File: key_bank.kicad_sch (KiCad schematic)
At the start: 2 parts, among them U4 MCP3208

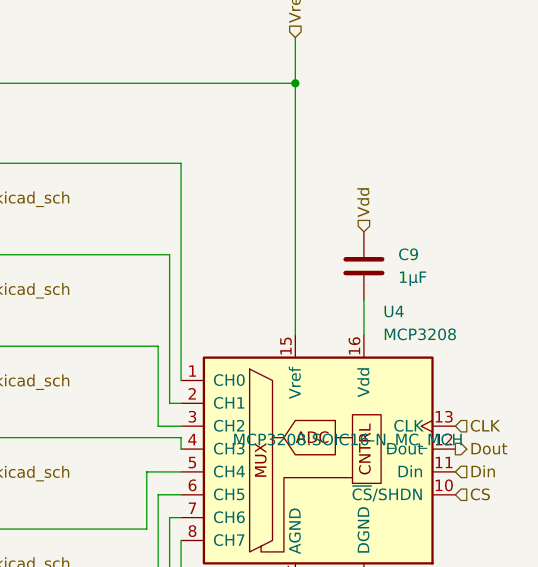
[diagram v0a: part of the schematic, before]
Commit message: [ADD](keys) added keys subsheet
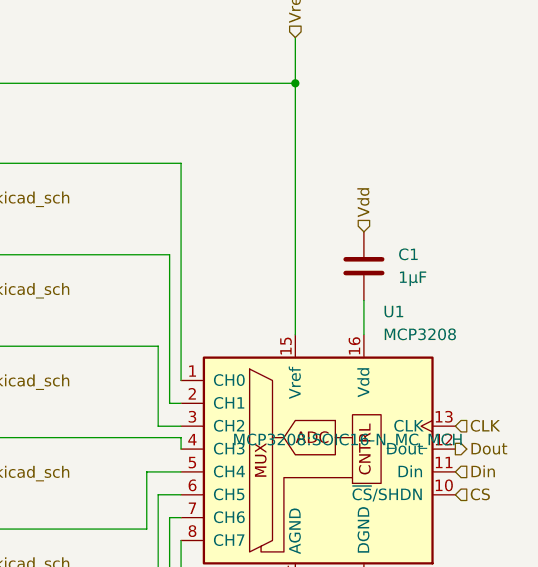
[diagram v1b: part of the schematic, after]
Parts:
- renumbered C9 to C1, U4 to U1

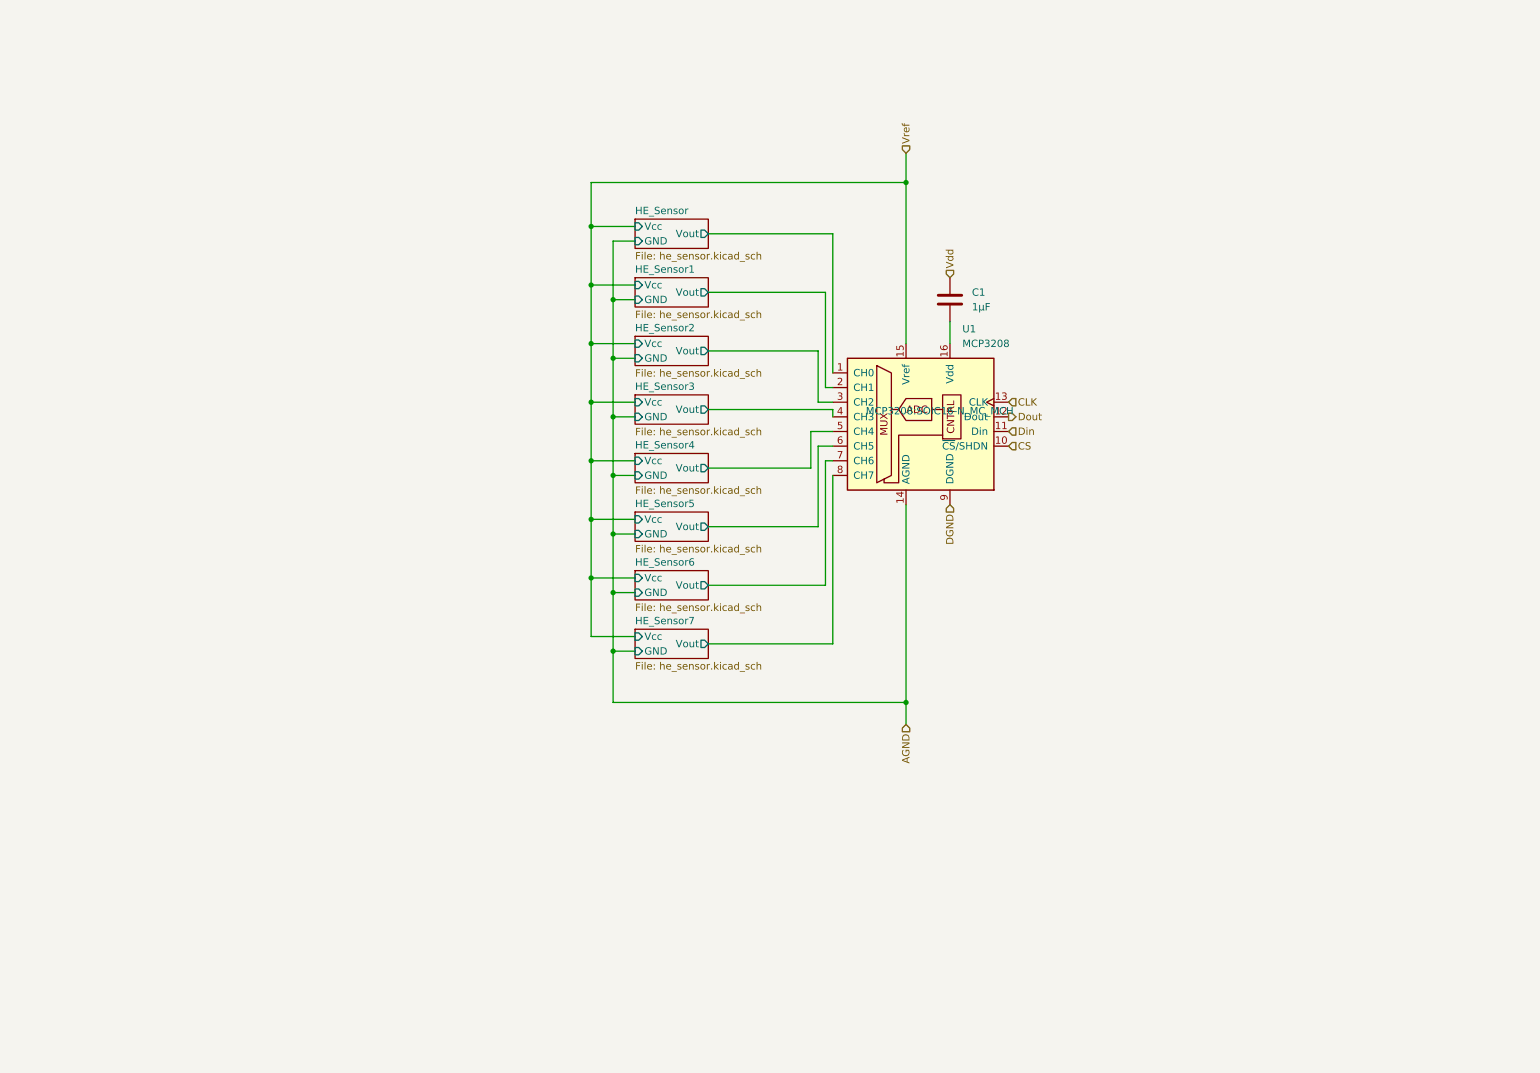
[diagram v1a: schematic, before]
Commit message: [UPDATE](TMR) switched to TMR sensors + added ldo
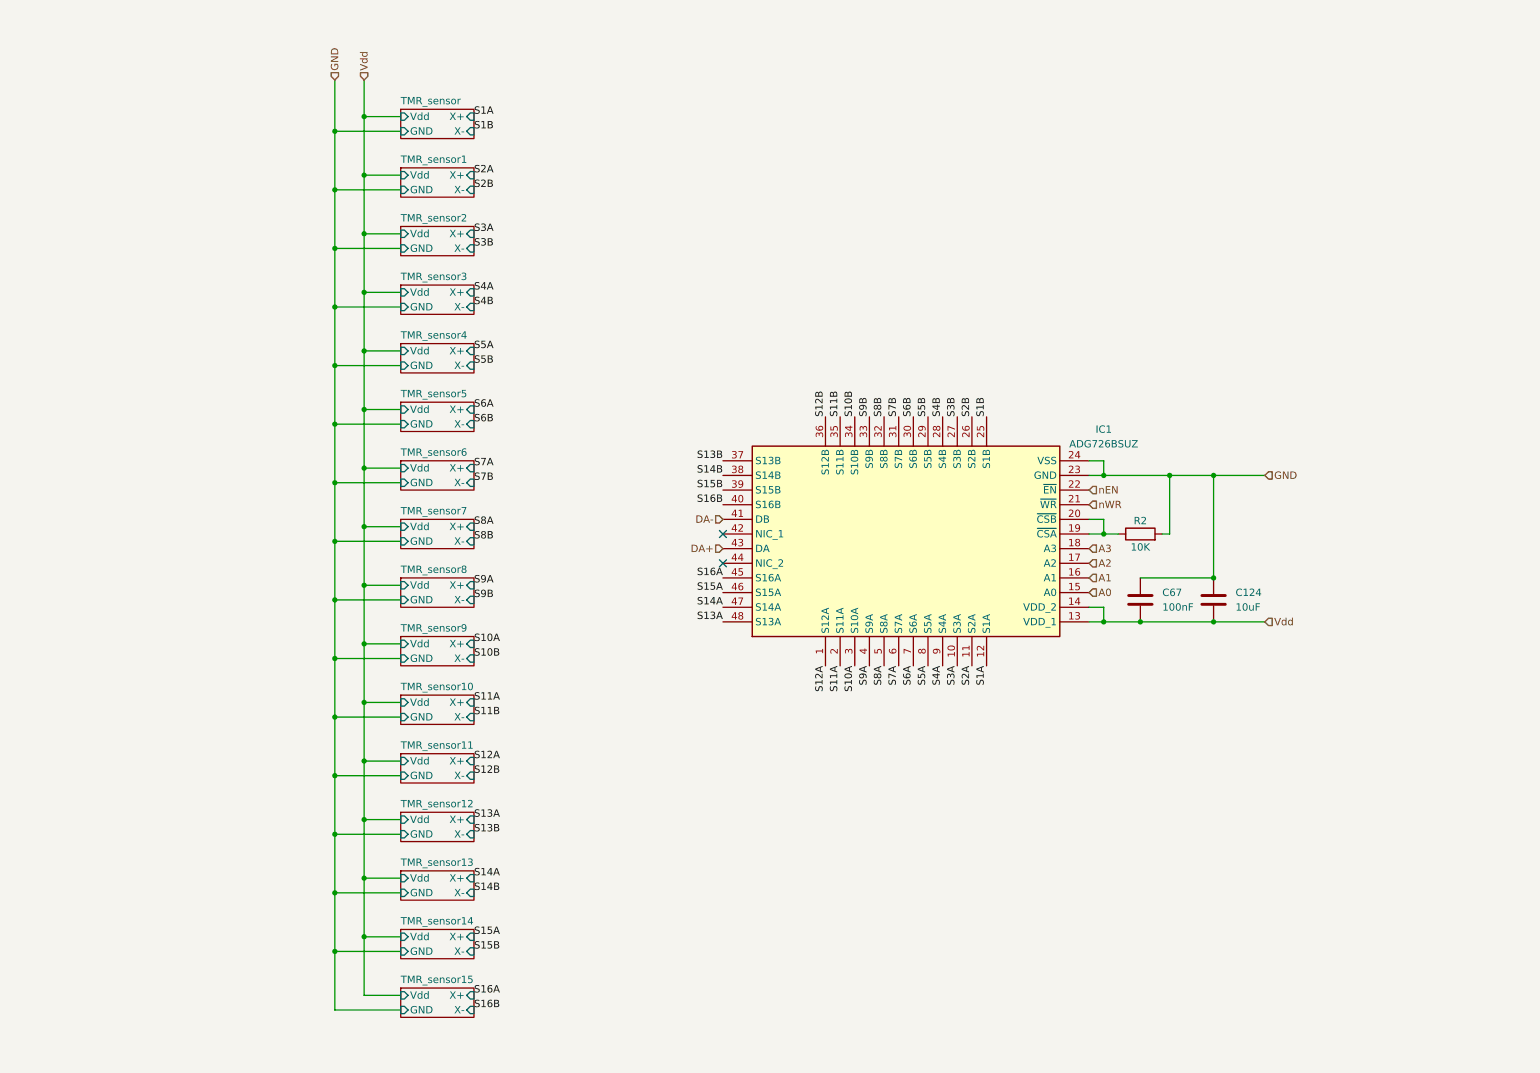
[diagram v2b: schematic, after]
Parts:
- removed C1: 1µF, symbol Device:C
- removed U1: MCP3208, MCP3208:SOIC16-N_MC_MCH, symbol Analog_ADC:MCP3208
- added C124: 10uF, symbol Device:C
- added C67: 100nF, symbol Device:C
- added IC1: ADG726BSUZ, QFP50P900X900X120-48N, symbol ADG726BSUZ:ADG726BSUZ
- added R2: 10K, symbol Device:R
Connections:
- net Vdd: now also C124.2, C67.2, IC1.13 (VDD_1), IC1.14 (VDD_2)
- new net: IC1.19 (~{CSA}), IC1.20 (~{CSB}), R2.1
- new net A0: IC1.15 (A0)
- new net A1: IC1.16 (A1)
- new net A2: IC1.17 (A2)
- new net A3: IC1.18 (A3)
- new net DA+: IC1.43 (DA)
- new net DA-: IC1.41 (DB)
- new net GND: C124.1, C67.1, IC1.23 (GND), IC1.24 (VSS), R2.2
- new net S10A: IC1.3 (S10A)
- new net S10B: IC1.34 (S10B)
- new net S11A: IC1.2 (S11A)
- new net S11B: IC1.35 (S11B)
- new net S12A: IC1.1 (S12A)
- new net S12B: IC1.36 (S12B)
- new net S13A: IC1.48 (S13A)
- new net S13B: IC1.37 (S13B)
- new net S14A: IC1.47 (S14A)
- new net S14B: IC1.38 (S14B)
- new net S15A: IC1.46 (S15A)
- new net S15B: IC1.39 (S15B)
- new net S16A: IC1.45 (S16A)
- new net S16B: IC1.40 (S16B)
- new net S1A: IC1.12 (S1A)
- new net S1B: IC1.25 (S1B)
- new net S2A: IC1.11 (S2A)
- new net S2B: IC1.26 (S2B)
- new net S3A: IC1.10 (S3A)
- new net S3B: IC1.27 (S3B)
- new net S4A: IC1.9 (S4A)
- new net S4B: IC1.28 (S4B)
- new net S5A: IC1.8 (S5A)
- new net S5B: IC1.29 (S5B)
- new net S6A: IC1.7 (S6A)
- new net S6B: IC1.30 (S6B)
- new net S7A: IC1.6 (S7A)
- new net S7B: IC1.31 (S7B)
- new net S8A: IC1.5 (S8A)
- new net S8B: IC1.32 (S8B)
- new net S9A: IC1.4 (S9A)
- new net S9B: IC1.33 (S9B)
- new net nEN: IC1.22 (~{EN})
- new net nWR: IC1.21 (~{WR})
- no-connect marks 0 -> 2
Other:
- removed sheet HE_Sensor
- removed sheet HE_Sensor1
- removed sheet HE_Sensor2
- removed sheet HE_Sensor3
- removed sheet HE_Sensor4
- removed sheet HE_Sensor5
- removed sheet HE_Sensor6
- removed sheet HE_Sensor7
- added sheet TMR_sensor (he_sensor.kicad_sch)
- added sheet TMR_sensor1 (he_sensor.kicad_sch)
- added sheet TMR_sensor10 (he_sensor.kicad_sch)
- added sheet TMR_sensor11 (he_sensor.kicad_sch)
- added sheet TMR_sensor12 (he_sensor.kicad_sch)
- added sheet TMR_sensor13 (he_sensor.kicad_sch)
- added sheet TMR_sensor14 (he_sensor.kicad_sch)
- added sheet TMR_sensor15 (he_sensor.kicad_sch)
- added sheet TMR_sensor2 (he_sensor.kicad_sch)
- added sheet TMR_sensor3 (he_sensor.kicad_sch)
- added sheet TMR_sensor4 (he_sensor.kicad_sch)
- added sheet TMR_sensor5 (he_sensor.kicad_sch)
- added sheet TMR_sensor6 (he_sensor.kicad_sch)
- added sheet TMR_sensor7 (he_sensor.kicad_sch)
- added sheet TMR_sensor8 (he_sensor.kicad_sch)
- added sheet TMR_sensor9 (he_sensor.kicad_sch)

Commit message: [ADD](General) v1
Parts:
- renumbered C67 to C14, C124 to C15, IC1 to IC2, R2 to R4
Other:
- note added: "Analog multiplexer"
- note added: "TMR sensors"
- company: (none) -> Ryzzen
- title: (none) -> TMR based triple USB Keyboard
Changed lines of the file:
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@@
 	(generator_version "9.0")
 	(paper "A4")
+	(title_block
+		(title "TMR based triple USB Keyboard")
+		(date "2025-12-28")
+		(rev "v1")
+		(company "Ryzzen")
+	)
+	(rectangle
+		(start 59.69 15.24)
+		(end 100.33 193.04)
+		(stroke
+			(width 0)
+			(type default)
+		)
+		(fill
+			(type none)
+		)
+	)
+	(rectangle
+		(start 123.19 72.39)
+		(end 237.49 138.43)
+		(stroke
+			(width 0)
+			(type default)
+		)
+		(fill
+			(type none)
+		)
+	)
+	(text "TMR sensors"
+		(exclude_from_sim no)
+		(at 110.998 17.018 0)
+		(effects
+			(font
+				(size 1.905 1.905)
+				(thickness 0.381)
+				(bold yes)
+			)
+		)
+	)
+	(text "Analog multiplexer"
+		(exclude_from_sim no)
+		(at 136.652 70.104 0)
+		(effects
+			(font
+				(size 1.905 1.905)
+				(thickness 0.381)
+				(bold yes)
+			)
+		)
+	)
 	(junction
 		(at 66.04 115.57)
@@
 		(dnp no)
 		(fields_autoplaced yes)
-		(property "Reference" "IC1"
+		(property "Reference" "IC2"
 			(at 199.39 85.9946 90)
 			(effects
@@
 				)
 				(path "/5d44d704-6136-40a8-98a4-93f001ea8743/c5dd3d76-8c7d-4253-bbc0-6b560edbfa92/3892192a-9e74-4718-aa5a-d4dfa6dc670f"
+					(reference "IC4")
+					(unit 1)
+				)
+				(path "/5d44d704-6136-40a8-98a4-93f001ea8743/c5dd3d76-8c7d-4253-bbc0-6b560edbfa92/735f3a62-f16a-407d-b596-d90350aa3066"
+					(reference "IC23")
+					(unit 1)
+				)
+				(path "/5d44d704-6136-40a8-98a4-93f001ea8743/c5dd3d76-8c7d-4253-bbc0-6b560edbfa92/7ffe2115-dd72-444b-89b3-b9005c9fe688"
+					(reference "IC44")
+					(unit 1)
+				)
+				(path "/5d44d704-6136-40a8-98a4-93f001ea8743/c5dd3d76-8c7d-4253-bbc0-6b560edbfa92/a1b59adb-224c-4a31-865b-1e7950bd0f40"
 					(reference "IC2")
 					(unit 1)
 				)
-				(path "/5d44d704-6136-40a8-98a4-93f001ea8743/c5dd3d76-8c7d-4253-bbc0-6b560edbfa92/735f3a62-f16a-407d-b596-d90350aa3066"
-					(reference "IC21")
-					(unit 1)
-				)
-				(path "/5d44d704-6136-40a8-98a4-93f001ea8743/c5dd3d76-8c7d-4253-bbc0-6b560edbfa92/7ffe2115-dd72-444b-89b3-b9005c9fe688"
-					(reference "IC22")
-					(unit 1)
-				)
-				(path "/5d44d704-6136-40a8-98a4-93f001ea8743/c5dd3d76-8c7d-4253-bbc0-6b560edbfa92/a1b59adb-224c-4a31-865b-1e7950bd0f40"
-					(reference "IC1")
-					(unit 1)
-				)
 				(path "/5d44d704-6136-40a8-98a4-93f001ea8743/c5dd3d76-8c7d-4253-bbc0-6b560edbfa92/cc77bec8-d3cc-43bb-b7a5-b3b6cadba114"
-					(reference "IC62")
+					(reference "IC78")
 					(unit 1)
 				)
@@
 		(on_board yes)
 		(dnp no)
-		(property "Reference" "R2"
+		(property "Reference" "R4"
 			(at 205.74 101.854 90)
 			(effects
@@
 			(project ""
 				(path "/5d44d704-6136-40a8-98a4-93f001ea8743/c5dd3d76-8c7d-4253-bbc0-6b560edbfa92/13b615a6-6b6e-4376-a5a5-45c5057b142a"
+					(reference "R8")
+					(unit 1)
+				)
+				(path "/5d44d704-6136-40a8-98a4-93f001ea8743/c5dd3d76-8c7d-4253-bbc0-6b560edbfa92/3892192a-9e74-4718-aa5a-d4dfa6dc670f"
+					(reference "R5")
+					(unit 1)
+				)
+				(path "/5d44d704-6136-40a8-98a4-93f001ea8743/c5dd3d76-8c7d-4253-bbc0-6b560edbfa92/735f3a62-f16a-407d-b596-d90350aa3066"
 					(reference "R6")
 					(unit 1)
 				)
-				(path "/5d44d704-6136-40a8-98a4-93f001ea8743/c5dd3d76-8c7d-4253-bbc0-6b560edbfa92/3892192a-9e74-4718-aa5a-d4dfa6dc670f"
-					(reference "R3")
+				(path "/5d44d704-6136-40a8-98a4-93f001ea8743/c5dd3d76-8c7d-4253-bbc0-6b560edbfa92/7ffe2115-dd72-444b-89b3-b9005c9fe688"
+					(reference "R7")
 					(unit 1)
 				)
-				(path "/5d44d704-6136-40a8-98a4-93f001ea8743/c5dd3d76-8c7d-4253-bbc0-6b560edbfa92/735f3a62-f16a-407d-b596-d90350aa3066"
+				(path "/5d44d704-6136-40a8-98a4-93f001ea8743/c5dd3d76-8c7d-4253-bbc0-6b560edbfa92/a1b59adb-224c-4a31-865b-1e7950bd0f40"
 					(reference "R4")
 					(unit 1)
 				)
-				(path "/5d44d704-6136-40a8-98a4-93f001ea8743/c5dd3d76-8c7d-4253-bbc0-6b560edbfa92/7ffe2115-dd72-444b-89b3-b9005c9fe688"
-					(reference "R5")
-					(unit 1)
-				)
-				(path "/5d44d704-6136-40a8-98a4-93f001ea8743/c5dd3d76-8c7d-4253-bbc0-6b560edbfa92/a1b59adb-224c-4a31-865b-1e7950bd0f40"
-					(reference "R2")
-					(unit 1)
-				)
 				(path "/5d44d704-6136-40a8-98a4-93f001ea8743/c5dd3d76-8c7d-4253-bbc0-6b560edbfa92/cc77bec8-d3cc-43bb-b7a5-b3b6cadba114"
-					(reference "R7")
+					(reference "R9")
 					(unit 1)
 				)
@@
 		(dnp no)
 		(fields_autoplaced yes)
-		(property "Reference" "C124"
+		(property "Reference" "C15"
 			(at 222.25 114.2999 0)
 			(effects
@@
 			(project "RyzzenKeyboard"
 				(path "/5d44d704-6136-40a8-98a4-93f001ea8743/c5dd3d76-8c7d-4253-bbc0-6b560edbfa92/13b615a6-6b6e-4376-a5a5-45c5057b142a"
-					(reference "C128")
+					(reference "C78")
 					(unit 1)
 				)
 				(path "/5d44d704-6136-40a8-98a4-93f001ea8743/c5dd3d76-8c7d-4253-bbc0-6b560edbfa92/3892192a-9e74-4718-aa5a-d4dfa6dc670f"
-					(reference "C125")
+					(reference "C18")
 					(unit 1)
 				)
 				(path "/5d44d704-6136-40a8-98a4-93f001ea8743/c5dd3d76-8c7d-4253-bbc0-6b560edbfa92/735f3a62-f16a-407d-b596-d90350aa3066"
-					(reference "C126")
+					(reference "C38")
 					(unit 1)
 				)
 				(path "/5d44d704-6136-40a8-98a4-93f001ea8743/c5dd3d76-8c7d-4253-bbc0-6b560edbfa92/7ffe2115-dd72-444b-89b3-b9005c9fe688"
-					(reference "C127")
+					(reference "C60")
 					(unit 1)
 				)
 				(path "/5d44d704-6136-40a8-98a4-93f001ea8743/c5dd3d76-8c7d-4253-bbc0-6b560edbfa92/a1b59adb-224c-4a31-865b-1e7950bd0f40"
-					(reference "C124")
+					(reference "C15")
 					(unit 1)
 				)
 				(path "/5d44d704-6136-40a8-98a4-93f001ea8743/c5dd3d76-8c7d-4253-bbc0-6b560edbfa92/cc77bec8-d3cc-43bb-b7a5-b3b6cadba114"
-					(reference "C129")
+					(reference "C96")
 					(unit 1)
 				)
@@
 		(dnp no)
 		(fields_autoplaced yes)
-		(property "Reference" "C67"
+		(property "Reference" "C14"
 			(at 209.55 114.2999 0)
 			(effects
@@
 			(project "RyzzenKeyboard"
 				(path "/5d44d704-6136-40a8-98a4-93f001ea8743/c5dd3d76-8c7d-4253-bbc0-6b560edbfa92/13b615a6-6b6e-4376-a5a5-45c5057b142a"
-					(reference "C122")
+					(reference "C77")
 					(unit 1)
 				)
 				(path "/5d44d704-6136-40a8-98a4-93f001ea8743/c5dd3d76-8c7d-4253-bbc0-6b560edbfa92/3892192a-9e74-4718-aa5a-d4dfa6dc670f"
-					(reference "C68")
+					(reference "C17")
 					(unit 1)
 				)
 				(path "/5d44d704-6136-40a8-98a4-93f001ea8743/c5dd3d76-8c7d-4253-bbc0-6b560edbfa92/735f3a62-f16a-407d-b596-d90350aa3066"
-					(reference "C120")
+					(reference "C37")
 					(unit 1)
 				)
 				(path "/5d44d704-6136-40a8-98a4-93f001ea8743/c5dd3d76-8c7d-4253-bbc0-6b560edbfa92/7ffe2115-dd72-444b-89b3-b9005c9fe688"
-					(reference "C121")
+					(reference "C59")
 					(unit 1)
 				)
 				(path "/5d44d704-6136-40a8-98a4-93f001ea8743/c5dd3d76-8c7d-4253-bbc0-6b560edbfa92/a1b59adb-224c-4a31-865b-1e7950bd0f40"
-					(reference "C67")
+					(reference "C14")
 					(unit 1)
 				)
 				(path "/5d44d704-6136-40a8-98a4-93f001ea8743/c5dd3d76-8c7d-4253-bbc0-6b560edbfa92/cc77bec8-d3cc-43bb-b7a5-b3b6cadba114"
-					(reference "C123")
+					(reference "C95")
 					(unit 1)
 				)
@@
 			(project "RyzzenKeyboard"
 				(path "/5d44d704-6136-40a8-98a4-93f001ea8743/c5dd3d76-8c7d-4253-bbc0-6b560edbfa92/a1b59adb-224c-4a31-865b-1e7950bd0f40"
-					(page "3")
+					(page "5")
 				)
 				(path "/5d44d704-6136-40a8-98a4-93f001ea8743/c5dd3d76-8c7d-4253-bbc0-6b560edbfa92/3892192a-9e74-4718-aa5a-d4dfa6dc670f"
@@
 			(project "RyzzenKeyboard"
 				(path "/5d44d704-6136-40a8-98a4-93f001ea8743/c5dd3d76-8c7d-4253-bbc0-6b560edbfa92/a1b59adb-224c-4a31-865b-1e7950bd0f40"
-					(page "15")
+					(page "101")
 				)
 				(path "/5d44d704-6136-40a8-98a4-93f001ea8743/c5dd3d76-8c7d-4253-bbc0-6b560edbfa92/3892192a-9e74-4718-aa5a-d4dfa6dc670f"

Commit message: [ADD](General) v2 split
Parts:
- added U10, U11, U12, U13, U14, U15, U16, U17, U18, U4, U5, U6, U7, U8, U9: ~, symbol switches:key_1
- added U3: ~, Switch_Keyboard_Cherry_MX:SW_Cherry_MX_PCB_Mag_1.00u, symbol switches:key_1
- renumbered C14 to C21, C15 to C22, R4 to R5
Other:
- note added: "Placeholder for switches footprints"
- moved on the sheet: C21, C22, IC2, R5

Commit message: [FIX](General) footprints
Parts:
- IC2: footprint QFP50P900X900X120-48N -> ADG726BSUZ:QFP50P900X900X120-48N
- renumbered R5 to R9, U9 to U10, U10 to U11, U11 to U12, U12 to U13, U13 to U14, U14 to U15, U15 to U16, U16 to U17, U17 to U18, U18 to U19, U3 to U4, U4 to U5, U5 to U6, U6 to U7, U7 to U8, U8 to U9

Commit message: [ADD](General) added all footprints expect leds
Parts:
- C21, C22: footprint (none) -> Capacitor_SMD:C_0603_1608Metric_Pad1.08x0.95mm_HandSolder
- R9: footprint (none) -> Resistor_SMD:R_0603_1608Metric_Pad0.98x0.95mm_HandSolder
- U10, U11, U12, U13, U14, U15, U16, U17, U18, U19, U5, U6, U7, U8, U9: footprint (none) -> Switch_Keyboard_Cherry_MX:SW_Cherry_MX_PCB_Mag_1.00u
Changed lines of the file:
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@@
 			)
 		)
-		(property "Footprint" ""
+		(property "Footprint" "Switch_Keyboard_Cherry_MX:SW_Cherry_MX_PCB_Mag_1.00u"
 			(at 54.61 30.48 0)
 			(effects
@@
 			)
 		)
-		(property "Footprint" ""
+		(property "Footprint" "Switch_Keyboard_Cherry_MX:SW_Cherry_MX_PCB_Mag_1.00u"
 			(at 54.61 132.08 0)
 			(effects
@@
 			)
 		)
-		(property "Footprint" ""
+		(property "Footprint" "Switch_Keyboard_Cherry_MX:SW_Cherry_MX_PCB_Mag_1.00u"
 			(at 29.21 81.28 0)
 			(effects
@@
 			)
 		)
-		(property "Footprint" ""
+		(property "Footprint" "Switch_Keyboard_Cherry_MX:SW_Cherry_MX_PCB_Mag_1.00u"
 			(at 29.21 106.68 0)
 			(effects
@@
 			)
 		)
-		(property "Footprint" ""
+		(property "Footprint" "Switch_Keyboard_Cherry_MX:SW_Cherry_MX_PCB_Mag_1.00u"
 			(at 29.21 182.88 0)
 			(effects
@@
 			)
 		)
-		(property "Footprint" ""
+		(property "Footprint" "Switch_Keyboard_Cherry_MX:SW_Cherry_MX_PCB_Mag_1.00u"
 			(at 54.61 106.68 0)
 			(effects
@@
 			)
 		)
-		(property "Footprint" ""
+		(property "Footprint" "Switch_Keyboard_Cherry_MX:SW_Cherry_MX_PCB_Mag_1.00u"
 			(at 54.61 55.88 0)
 			(effects
@@
 			)
 		)
-		(property "Footprint" ""
+		(property "Footprint" "Resistor_SMD:R_0603_1608Metric_Pad0.98x0.95mm_HandSolder"
 			(at 241.3 104.648 90)
 			(effects
@@
 			)
 		)
-		(property "Footprint" ""
+		(property "Footprint" "Switch_Keyboard_Cherry_MX:SW_Cherry_MX_PCB_Mag_1.00u"
 			(at 29.21 132.08 0)
 			(effects
@@
 			)
 		)
-		(property "Footprint" ""
+		(property "Footprint" "Switch_Keyboard_Cherry_MX:SW_Cherry_MX_PCB_Mag_1.00u"
 			(at 80.01 55.88 0)
 			(effects
@@
 			)
 		)
-		(property "Footprint" ""
+		(property "Footprint" "Switch_Keyboard_Cherry_MX:SW_Cherry_MX_PCB_Mag_1.00u"
 			(at 29.21 55.88 0)
 			(effects
@@
 			)
 		)
-		(property "Footprint" ""
+		(property "Footprint" "Switch_Keyboard_Cherry_MX:SW_Cherry_MX_PCB_Mag_1.00u"
 			(at 29.21 157.48 0)
 			(effects
@@
 			)
 		)
-		(property "Footprint" ""
+		(property "Footprint" "Switch_Keyboard_Cherry_MX:SW_Cherry_MX_PCB_Mag_1.00u"
 			(at 54.61 81.28 0)
 			(effects
@@
 			)
 		)
-		(property "Footprint" ""
+		(property "Footprint" "Switch_Keyboard_Cherry_MX:SW_Cherry_MX_PCB_Mag_1.00u"
 			(at 54.61 182.88 0)
 			(effects
@@
 			)
 		)
-		(property "Footprint" ""
+		(property "Footprint" "Capacitor_SMD:C_0603_1608Metric_Pad1.08x0.95mm_HandSolder"
 			(at 254.9652 118.11 0)
 			(effects
@@
 			)
 		)
-		(property "Footprint" ""
+		(property "Footprint" "Capacitor_SMD:C_0603_1608Metric_Pad1.08x0.95mm_HandSolder"
 			(at 242.2652 118.11 0)
 			(effects
@@
 			)
 		)
-		(property "Footprint" ""
+		(property "Footprint" "Switch_Keyboard_Cherry_MX:SW_Cherry_MX_PCB_Mag_1.00u"
 			(at 54.61 157.48 0)
 			(effects
@@
 			)
 		)
-		(property "Footprint" ""
+		(property "Footprint" "Switch_Keyboard_Cherry_MX:SW_Cherry_MX_PCB_Mag_1.00u"
 			(at 80.01 30.48 0)
 			(effects
